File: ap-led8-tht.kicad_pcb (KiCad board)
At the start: 2 copper layers, 36.6 x 16.1 mm, 12 parts, among them J1 Conn_01x08_Socket, J2 Conn_01x08_Socket

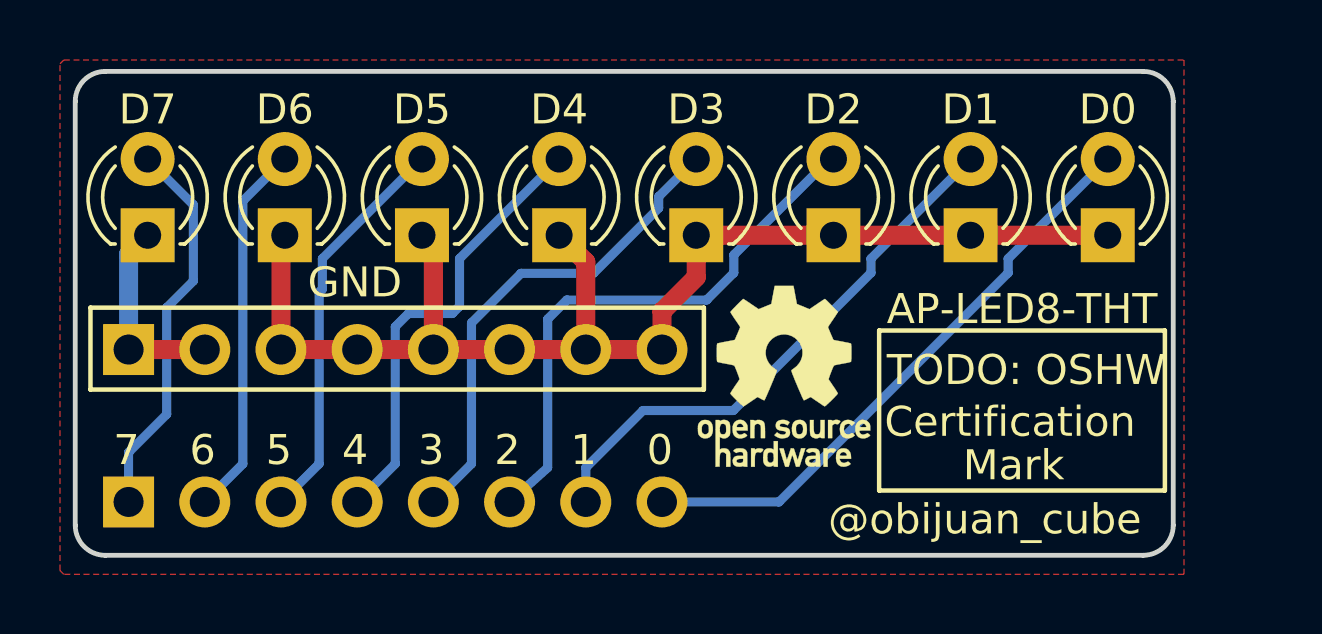
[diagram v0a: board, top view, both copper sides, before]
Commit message: add certification mark footprint
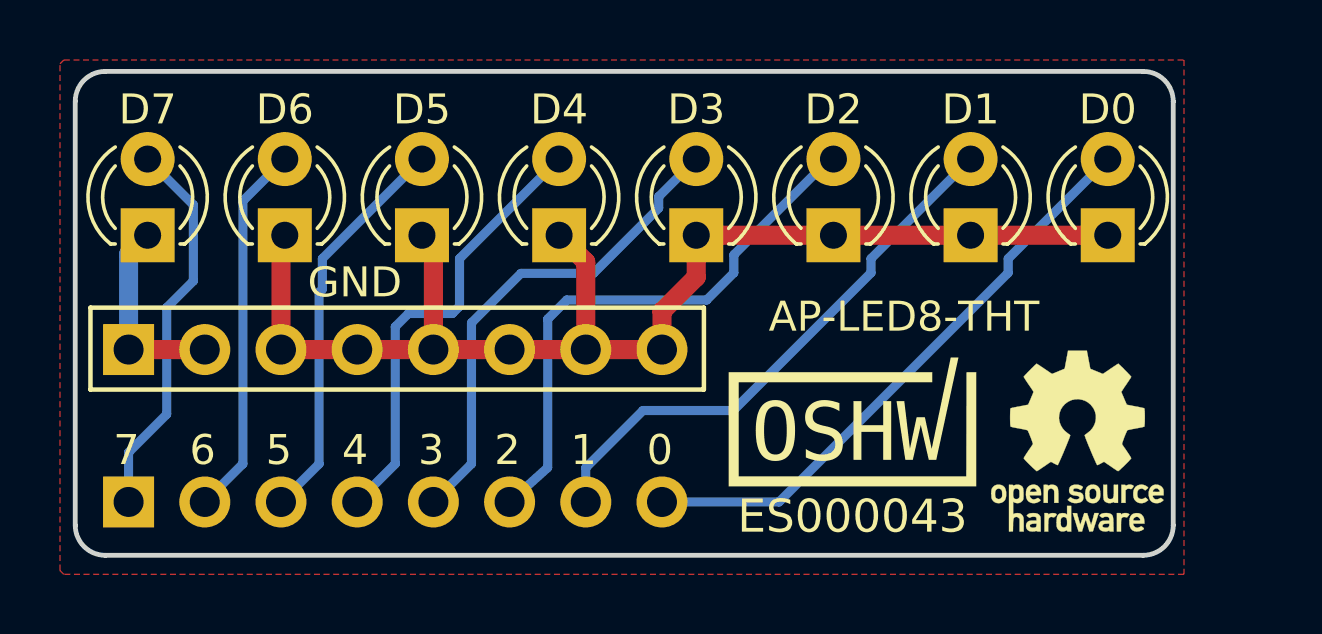
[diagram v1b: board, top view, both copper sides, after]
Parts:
- added REF**: OSHW-Certification-Mark-Stacked_8x7mm_SilkScreen, Monolito:OSHW-Certification-Mark-Stacked_8x7mm_SilkScreen, F.Cu at (104.1, 61.6)
- moved REF** 10.0 mm to (111.6, 61.5)
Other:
- board text removed: "Certification"
- board text removed: "Mark"
- board text removed: "TODO: OSHW"
